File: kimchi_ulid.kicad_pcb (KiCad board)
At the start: 4 copper layers, 65 x 32 mm, 8 parts, among them J1 DF40HC(3.5)-60DS, J2 DF40HC(3.5)-60DS, U1 24C32

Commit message: Board Shape
Added board shape and mocked up location of Kimchi module and lipo battery solution.
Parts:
- moved H1 20.0 mm to (118.5, 77.9)
- moved H2 20.0 mm to (118.5, 102.1)
- moved H3 20.0 mm to (142.6, 77.9)
- moved H4 20.0 mm to (142.6, 102.1)
- moved J1 20.0 mm to (152.5, 77.0)
- moved J2 20.0 mm to (152.5, 103.0)
- moved LOGO1 20.0 mm to (111.5, 102.0)
- moved U1 20.0 mm to (169.0, 77.5)
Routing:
- removed copper zone on B.Cu, net GND
- removed copper zone on In1.Cu, net GND
- removed copper zone on In2.Cu, net VDD_3V3
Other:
- board size 65 x 32 mm -> 209.3 x 89.3 mm
- board text added: "LITHIUM POLYMER BATTERY"

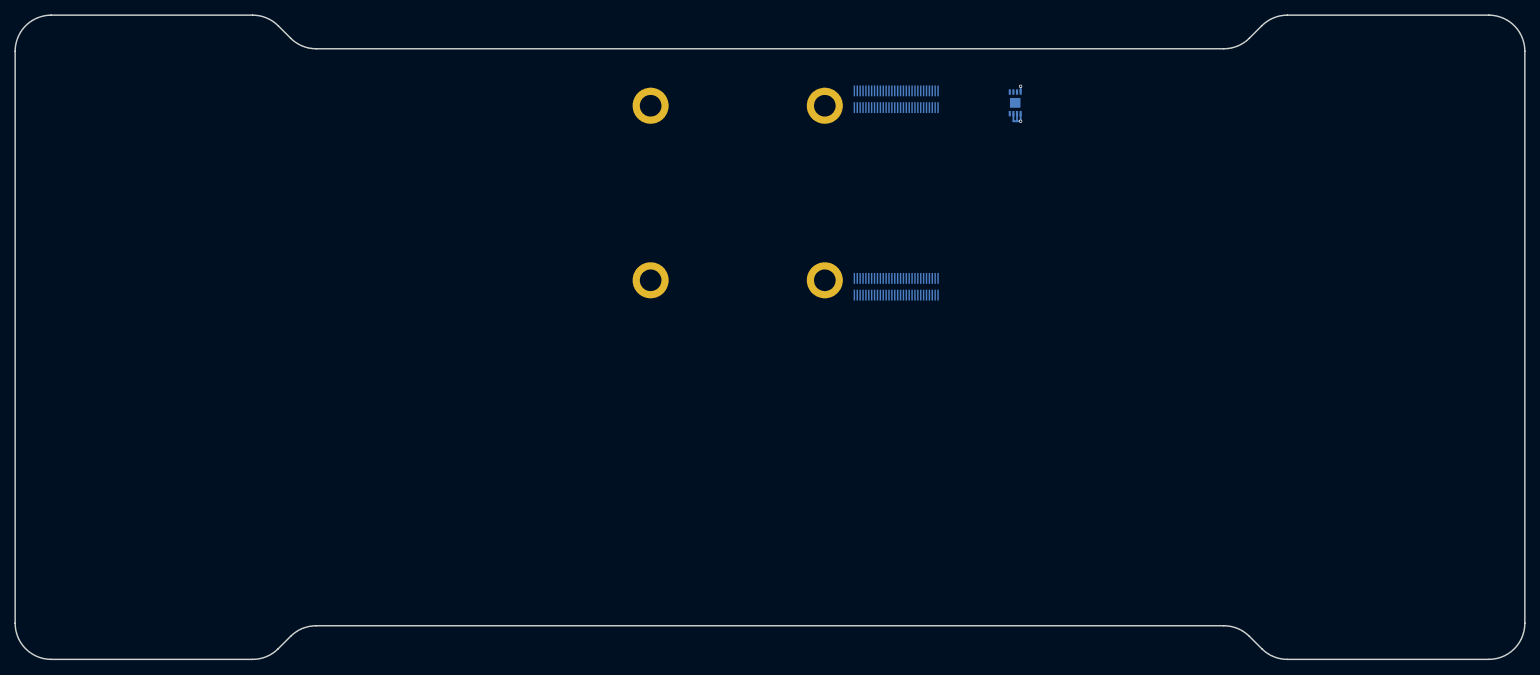
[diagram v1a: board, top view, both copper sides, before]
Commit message: Mockup Progress
Added standard SMT tactile switches to represent the button pad layout for both D-Pad and Face Buttons. Added dummy Analog Sticks for mockup purposes until we can get samples of the Nintendo Switch Joy Con replacement sticks. Also added USB port and Audio Codec/Headset jack, currently working through codec shecmatic implemenation.
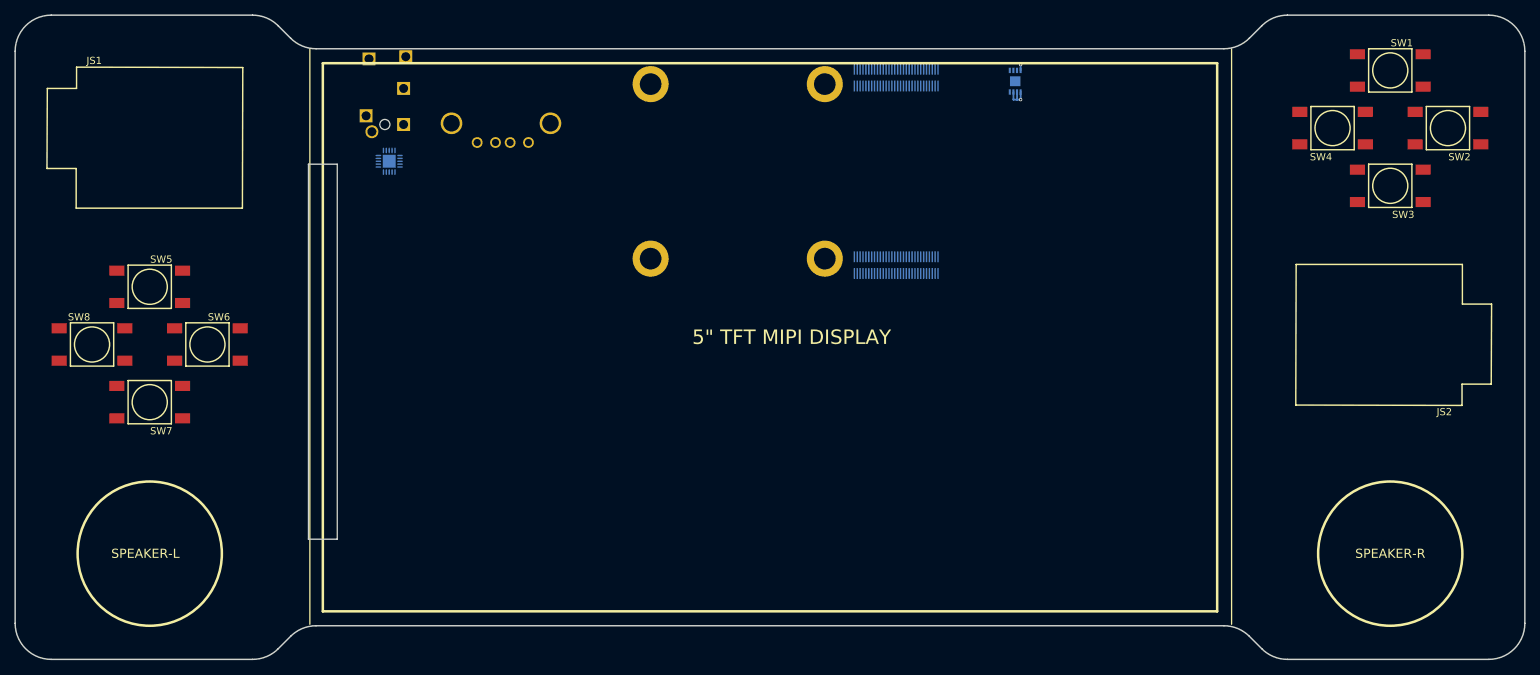
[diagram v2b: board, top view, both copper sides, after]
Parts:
- added J3: KUSBX-AS1N-B, kimchi_ulid:USB_A, B.Cu at (94.4, 83.0)
- added J4: 54-00176, kimchi_ulid:54-00176, B.Cu at (81.6, 70.0)
- added J5: SGTL5000XNLA3, kimchi_ulid:QFN40P300X300X60-21N, B.Cu at (82.2, 85.6)
- added JS1: Keyes_HW-504, kimchi_ulid:Keyes_JoyStick, F.Cu at (48.8, 81.0)
- added JS2: Keyes_HW-504, kimchi_ulid:Keyes_JoyStick, F.Cu at (221.0, 111.0)
- added SW1: TL3301NF260QG, kimchi_ulid:TL3301NF260QG, F.Cu at (221.0, 73.0)
- added SW2: TL3301NF260QG, kimchi_ulid:TL3301NF260QG, F.Cu at (229.0, 81.0)
- added SW3: TL3301NF260QG, kimchi_ulid:TL3301NF260QG, F.Cu at (221.0, 89.0)
- added SW4: TL3301NF260QG, kimchi_ulid:TL3301NF260QG, F.Cu at (213.0, 81.0)
- added SW5: TL3301NF260QG, kimchi_ulid:TL3301NF260QG, F.Cu at (49.0, 103.0)
- added SW6: TL3301NF260QG, kimchi_ulid:TL3301NF260QG, F.Cu at (57.0, 111.0)
- added SW7: TL3301NF260QG, kimchi_ulid:TL3301NF260QG, F.Cu at (49.0, 119.0)
- added SW8: TL3301NF260QG, kimchi_ulid:TL3301NF260QG, F.Cu at (41.0, 111.0)
- moved H1 3.00 mm to (118.5, 74.9)
- moved H2 3.00 mm to (118.5, 99.1)
- moved H3 3.00 mm to (142.6, 74.9)
- moved H4 3.00 mm to (142.6, 99.1)
- moved J1 3.00 mm to (152.5, 74.0)
- moved J2 3.00 mm to (152.5, 100.0)
- moved LOGO1 3.00 mm to (111.5, 99.0)
- moved U1 3.00 mm to (169.0, 74.5)
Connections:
- J1 pad 1: (no net) -> /USDHC3_CMD
- J1 pad 17: (no net) -> I2C3_SDA
- J1 pad 18: (no net) -> I2C3_SCL
- J1 pad 19: (no net) -> I2C2_SDA
- J1 pad 2: (no net) -> /USDHC3_CLK
- J1 pad 20: (no net) -> I2C2_SCL
- J1 pad 21: (no net) -> I2C1_SDA
- J1 pad 22: (no net) -> I2C1_SCL
- J1 pad 23: (no net) -> ECSPI1_SCLK
- J1 pad 24: (no net) -> ECSPI1_SS0
- J1 pad 25: (no net) -> ECSPI1_MOSI
- J1 pad 26: (no net) -> ECSPI1_MISO
- J1 pad 27: (no net) -> ECSPI2_SCLK
- J1 pad 28: (no net) -> ECSPI2_SS0
- J1 pad 29: (no net) -> ECSPI2_MOSI
- J1 pad 3: (no net) -> /USDHC3_DATA3
- J1 pad 30: (no net) -> ECSPI2_MISO
- J1 pad 31: (no net) -> /DISP_D0_N
- J1 pad 32: (no net) -> /DISP_D0_P
- J1 pad 33: (no net) -> /DISP_D1_N
- J1 pad 34: (no net) -> /DISP_D1_P
- J1 pad 35: (no net) -> /DISP_CK_N
- J1 pad 36: (no net) -> /DISP_CK_P
- J1 pad 37: (no net) -> /DISP_D2_N
- J1 pad 38: (no net) -> /DISP_D2_P
- J1 pad 39: (no net) -> /DISP_D3_N
- J1 pad 4: (no net) -> /USDHC3_DATA0
- J1 pad 40: (no net) -> /DISP_D3_P
- J1 pad 41: (no net) -> /CAM_D0_N
- J1 pad 42: (no net) -> /CAM_D0_P
- J1 pad 43: (no net) -> /CAM_D1_N
- J1 pad 44: (no net) -> /CAM_D1_P
- J1 pad 45: (no net) -> /CAM_CK_N
- J1 pad 46: (no net) -> /CAM_CK_P
- J1 pad 47: (no net) -> /CAM_D2_N
- J1 pad 48: (no net) -> /CAM_D2_P
- J1 pad 49: (no net) -> /CAM_D3_N
- J1 pad 5: (no net) -> /USDHC3_DATA1
- J1 pad 50: (no net) -> /CAM_D3_P
- J1 pad 52: (no net) -> UIM_VPP
- J1 pad 53: (no net) -> UIM_RESET_N
- J1 pad 54: (no net) -> UIM_CLK
- J1 pad 55: (no net) -> UIM_DATA
- J1 pad 56: (no net) -> UIM_PWR
- J1 pad 57: (no net) -> USB2_VBUS
- J1 pad 58: (no net) -> USB2_ID
- J1 pad 59: (no net) -> USB2_DN
- J1 pad 6: (no net) -> /USDHC3_DATA2
- J1 pad 60: (no net) -> USB2_DP
- J2 pad 1: (no net) -> /ENET_MDIO
- J2 pad 10: (no net) -> /ENET_TD0
- J2 pad 11: (no net) -> /ENET_TD3
- J2 pad 12: (no net) -> /ENET_TD2
- J2 pad 13: (no net) -> /ENET_TX_CTL
- J2 pad 14: (no net) -> /ENET_TXC
- J2 pad 15: (no net) -> SAI2_RXD0
- J2 pad 16: (no net) -> SAI2_TXFS
- J2 pad 17: (no net) -> SAI2_RXC
- J2 pad 18: (no net) -> SAI2_TXD0
- J2 pad 19: (no net) -> SAI2_TXC
- J2 pad 2: (no net) -> /ENET_MDC
- J2 pad 20: (no net) -> SAI2_MCLK
- J2 pad 21: (no net) -> SAI2_RXFS
- J2 pad 22: (no net) -> GPIO1[15]
- J2 pad 23: (no net) -> GPIO1[14]
- J2 pad 24: (no net) -> GPIO1[13]
- J2 pad 25: (no net) -> GPIO1[12]
- J2 pad 26: (no net) -> GPIO1[11]
- J2 pad 27: (no net) -> GPIO1[10]
- J2 pad 28: (no net) -> GPIO1[9]
- J2 pad 29: (no net) -> GPIO1[1]
- J2 pad 3: (no net) -> /ENET_RD3
- J2 pad 30: (no net) -> GPIO1[0]
- J2 pad 31: (no net) -> SAI3_TXC
- J2 pad 32: (no net) -> SAI3_TXD
- J2 pad 33: (no net) -> SAI3_RXD
- J2 pad 34: (no net) -> SAI3_RXFS
- J2 pad 35: (no net) -> SAI3_RXC
- J2 pad 36: (no net) -> SAI3_TXFS
- J2 pad 37: (no net) -> SAI3_MCLK
- J2 pad 4: (no net) -> /ENET_RD1
- J2 pad 46: (no net) -> UART1_TX
- J2 pad 47: (no net) -> UART1_RX
- J2 pad 48: (no net) -> UART3_TX
- J2 pad 49: (no net) -> UART3_RX
- J2 pad 5: (no net) -> /ENET_RD2
- J2 pad 58: (no net) -> Net-(J2-Pad58)
- J2 pad 59: (no net) -> PCIE_USB_D_P
- J2 pad 6: (no net) -> /ENET_RD0
- J2 pad 60: (no net) -> PCIE_USB_D_N
- J2 pad 7: (no net) -> /ENET_RXC
- J2 pad 8: (no net) -> /ENET_RX_CTL
- J2 pad 9: (no net) -> /ENET_TD1
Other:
- outline, holes or cut-outs redrawn
- board text added: "5" TFT MIPI DISPLAY"
- board text added: "SPEAKER-L"
- board text added: "SPEAKER-R"
